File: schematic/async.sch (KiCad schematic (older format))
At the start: 84 parts, among them J1 LOAD, J2 Solar panel, J3 Battery, J4 Screw_Terminal_01x03, J5 Temperature, J7 Screw_Terminal_01x03, J8 USB_B, Q1 IRF4905, Q2 IRF4905, Q3 IRF4905, Q4 2N3904, Q5 2N3904, Q6 IRF4905, Q7 2N3904, Q8 IRF4905, Q9 2N3904, SW1 Backlight control, SW2 RESET, T1 Mains Transformer, U1 ACS712module, U10 ATMEGA328-PU, U11 SD_Micro_5V, U2 IR2110, U3 IR2110, U4 DS18B20, U5 ACS712module, U6 DS18B20, U7 DS1307_RTC, U8 MP2307_DC-DC_module, U9 LCDSerial2004

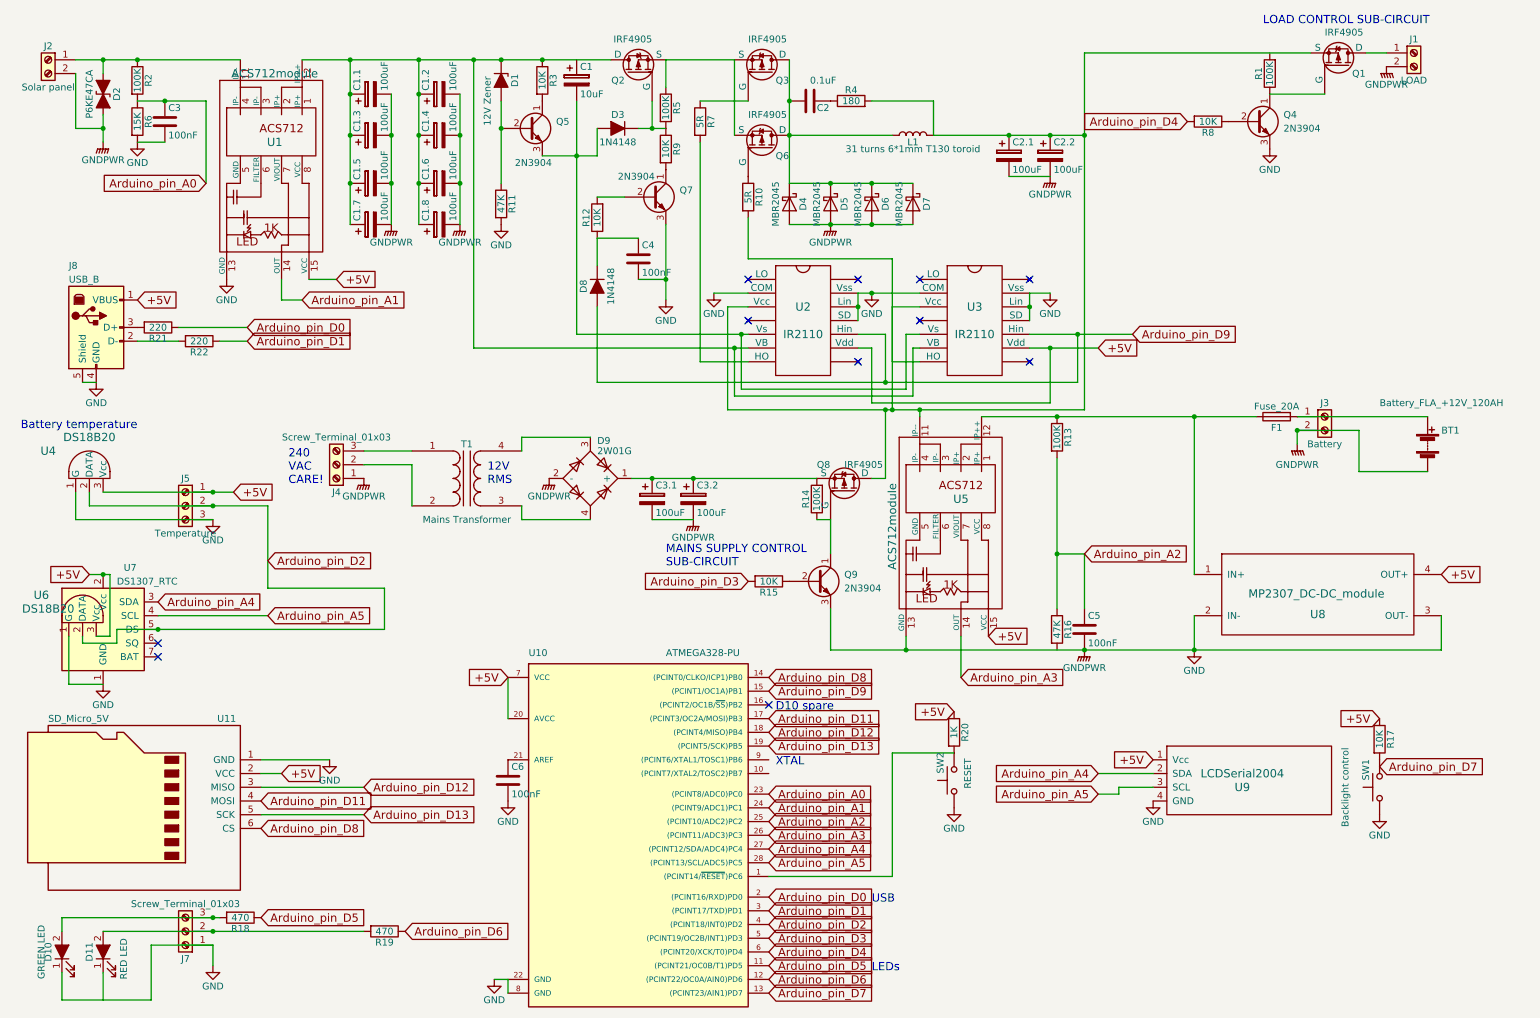
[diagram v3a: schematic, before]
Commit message: added 16 MHz crystal and mains 12V terminals
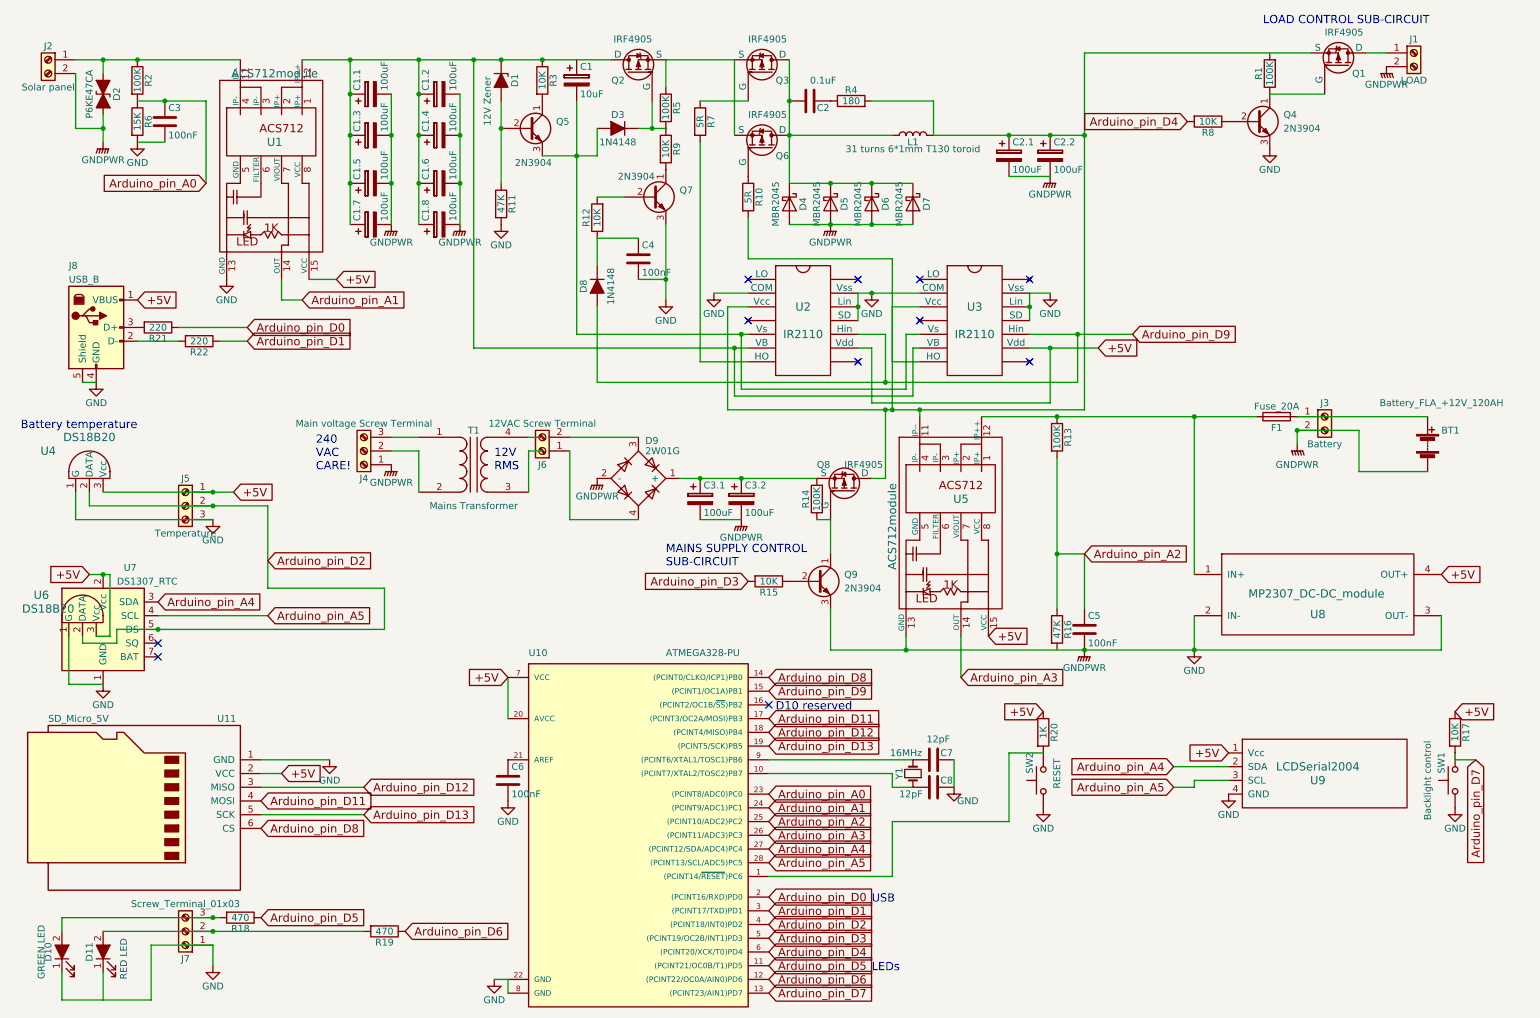
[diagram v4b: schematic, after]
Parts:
- added C7, C8: 12pF, symbol C
- added J6: 12VAC Screw Terminal, symbol Screw_Terminal_01x02
- added Y1: 16MHz, symbol Crystal_Small
- J4: value Screw_Terminal_01x03 -> Main voltage Screw Terminal
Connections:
- net Arduino_pin_D7: now also R17.2, SW1.2
- net GND: now also C7.1, C8.1
- net at U10.10 ((PCINT7/XTAL2/TOSC2)PB7): now also C8.2, Y1.1
- net at U10.9 ((PCINT6/XTAL1/TOSC1)PB6): now also C7.2, Y1.2
- net at T1.3 (SA): no longer D9.4
- net at T1.4 (SB): no longer D9.3
- new net: D9.3, J6.2 (Pin_2)
- new net: D9.4, J6.1 (Pin_1)
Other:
- note added: "D10 reserved"
- note removed: "D10 spare"
- note removed: "XTAL"
- moved on the sheet: C3.1, C3.2, D9, J4, R17, R20, SW1, SW2, T1, U9

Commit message: swapped C1.x and Q1
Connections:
- net at C1.1.1, C1.2.1, C1.3.1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: now also Q2.3 (S), Q3.3 (S), Q6.3 (S), R5.1; no longer D1.1 (K), Q2.1 (D), R3.1, U1.12 (IP++), U2.6 (VB), U3.6 (VB)
- net at C2.1.1, C2.2.1, L1.2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: no longer R10.2, U3.7 (HO)
- new net: D1.1 (K), Q2.1 (D), R3.1, U1.12 (IP++), U2.6 (VB), U3.6 (VB)
- new net: R10.2, U3.7 (HO)
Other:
- moved on the sheet: C1, C1.1, C1.2, C1.3, C1.4, C1.5, C1.6, C1.7, C1.8, C4, D1, D3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

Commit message: updated BOM
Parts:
- renumbered C7 to C10, C8 to C11, C1 to C7, C2 to C8, C3 to C9
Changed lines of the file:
@@
 $EndComp
 $Comp
-L C C3
+L C C9
 U 1 1 5AF665D7
 P 1550 1300
-F 0 "C3" H 1575 1400 50  0000 L CNN
+F 0 "C9" H 1575 1400 50  0000 L CNN
 F 1 "100nF" H 1575 1200 50  0000 L CNN
 F 2 "" H 1588 1150 50  0001 C CNN
@@
 $EndComp
 Wire Wire Line
-	1350 1150 1550 1150
-Wire Wire Line
-	1550 1150 1850 1150
-Wire Wire Line
-	900  850  1100 850
-Wire Wire Line
-	1100 850  1350 850
-Wire Wire Line
-	1350 850  2100 850
+	1350 1150 1850 1150
+Wire Wire Line
+	900  850  2100 850
 $Comp
 L GND #PWR3
@@
 Connection ~ 9800 3550
 Wire Wire Line
-	4300 850  4450 850
-Wire Wire Line
-	4450 850  4950 850
-Wire Wire Line
-	4950 850  5700 850
-Wire Wire Line
-	2550 850  2900 850
-Wire Wire Line
-	2900 850  3100 850
-Wire Wire Line
-	3100 850  3400 850
-Wire Wire Line
-	3400 850  3900 850
+	4300 850  5700 850
+Wire Wire Line
+	2550 850  3900 850
 $Comp
 L GNDPWR #PWR21
@@
 Arduino_pin_D2
 Wire Wire Line
-	1000 4100 1900 4100
-Wire Wire Line
-	1900 4100 2300 4100
+	1000 4100 2300 4100
 $Comp
 L GND #PWR19
@@
 +5V
 Wire Wire Line
-	1100 4000 1900 4000
-Wire Wire Line
-	1900 4000 2050 4000
+	1100 4000 2050 4000
 Wire Wire Line
 	1000 4000 1000 4100
@@
 	900  1350 900  950
 Wire Wire Line
-	1100 1250 1100 1350
-Wire Wire Line
-	1100 1350 1100 1450
+	1100 1250 1100 1450
 Wire Wire Line
 	1100 950  1100 850
@@
 $EndComp
 Wire Wire Line
-	6400 5150 6950 5150
-Wire Wire Line
-	6950 5150 8250 5150
-Wire Wire Line
-	8250 5150 9050 5150
-Wire Wire Line
-	9050 5150 10850 5150
+	6400 5150 10850 5150
 $Comp
 L GND #PWR22
@@
 MAINS SUPPLY CONTROL \nSUB-CIRCUIT
 Wire Wire Line
-	7500 3450 8050 3450
-Wire Wire Line
-	8050 3450 9050 3450
-Wire Wire Line
-	9050 3450 9500 3450
+	7500 3450 9500 3450
 $Comp
 L ACS712module U5
@@
 $EndComp
 Wire Wire Line
-	8050 3750 8050 4450
-Wire Wire Line
-	8050 4450 8050 4850
+	8050 3750 8050 4850
 Wire Wire Line
 	6950 5050 6950 5150
@@
 Arduino_pin_D7
 Wire Wire Line
-	4450 850  4450 1100
-Wire Wire Line
-	4450 1100 4450 1400
-Wire Wire Line
-	4450 1400 4450 1750
-Wire Wire Line
-	4450 1750 4450 2050
+	4450 850  4450 2050
 Connection ~ 4450 1750
 Connection ~ 4450 1400
@@
 Connection ~ 4450 1100
 Wire Wire Line
-	4750 1100 4750 1400
-Wire Wire Line
-	4750 1400 4750 1750
-Wire Wire Line
-	4750 1750 4750 2050
+	4750 1100 4750 2050
 Connection ~ 4750 1400
 Connection ~ 4750 1750
 Wire Wire Line
-	8250 3400 7050 3400
-Wire Wire Line
-	7050 3400 6850 3400
-Wire Wire Line
-	6850 3400 6800 3400
-Wire Wire Line
-	6800 3400 5650 3400
+	8250 3400 5650 3400
 Wire Wire Line
 	7050 3400 7050 3450
@@
 	2300 4700 3150 4700
 Wire Wire Line
-	3150 4700 3150 5000
-Wire Wire Line
-	3150 5000 1500 5000
-Wire Wire Line
-	1500 5000 1200 5000
+	3150 5000 3150 4700
+Wire Wire Line
+	1200 5000 3150 5000
 $Comp
 L DS18B20 U6
@@
 	1050 5050 1150 5050
 Wire Wire Line
-	1150 5050 1150 4600
-Wire Wire Line
-	1150 4600 1100 4600
-Wire Wire Line
-	1100 4600 1000 4600
+	1150 4600 1150 5050
+Wire Wire Line
+	1000 4600 1150 4600
 Wire Wire Line
 	950  5050 950  5100
@@
 $EndComp
 Wire Wire Line
-	800  7100 1900 7100
-Wire Wire Line
-	1900 7100 1950 7100
-Wire Wire Line
-	1100 7200 1900 7200
-Wire Wire Line
-	1900 7200 3000 7200
+	800  7100 1950 7100
+Wire Wire Line
+	1100 7200 3000 7200
 Connection ~ 1900 7200
 Wire Wire Line
@@
 $EndComp
 Wire Wire Line
-	8250 800  8250 1400
-Wire Wire Line
-	8250 1400 8250 3400
+	8250 800  8250 3400
 $Comp
 L ATMEGA328-PU U10
@@
 $EndComp
 $Comp
-L GNDPWR #PWR6
+L GNDPWR #PWR7
 U 1 1 5AFA9065
 P 4750 2050
-F 0 "#PWR6" H 4750 1850 50  0001 C CNN
+F 0 "#PWR7" H 4750 1850 50  0001 C CNN
 F 1 "GNDPWR" H 4750 1920 50  0000 C CNN
 F 2 "" H 4750 2000 50  0001 C CNN
@@
 $EndComp
 Wire Wire Line
-	4100 1350 4200 1350
-Wire Wire Line
-	4200 1350 4300 1350
+	4100 1350 4300 1350
 Wire Wire Line
 	4200 1350 4200 1150
@@
 $EndComp
 Wire Wire Line
-	3100 1150 3100 1350
-Wire Wire Line
-	3100 1350 3100 1750
-$Comp
-L CP C1
+	3100 1150 3100 1750
+$Comp
+L CP C7
 U 1 1 5AFAF73D
 P 3650 1000
-F 0 "C1" H 3675 1100 50  0000 L CNN
+F 0 "C7" H 3675 1100 50  0000 L CNN
 F 1 "10uF" H 3675 900 50  0000 L CNN
 F 2 "" H 3688 850 50  0001 C CNN
@@
 $EndComp
 $Comp
-L GND #PWR8
+L GND #PWR6
 U 1 1 5AFAF73F
 P 3100 2050
-F 0 "#PWR8" H 3100 1800 50  0001 C CNN
+F 0 "#PWR6" H 3100 1800 50  0001 C CNN
 F 1 "GND" H 3100 1900 50  0000 C CNN
 F 2 "" H 3100 2050 50  0001 C CNN
@@
 $EndComp
 Wire Wire Line
-	3400 1550 3650 1550
-Wire Wire Line
-	3650 1550 3800 1550
+	3400 1550 3800 1550
 Wire Wire Line
 	4300 850  4300 1050
@@
 $EndComp
 Wire Wire Line
-	5700 1400 5700 850
-Wire Wire Line
-	6100 850  6100 1150
-Wire Wire Line
-	6100 1150 6100 1400
-Wire Wire Line
-	6100 1400 6100 1750
+	5700 850  5700 1400
+Wire Wire Line
+	6100 850  6100 1750
 Wire Wire Line
 	6100 1400 6850 1400
@@
 $EndComp
 Wire Wire Line
-	6100 1750 6400 1750
-Wire Wire Line
-	6400 1750 6700 1750
-Wire Wire Line
-	6700 1750 7000 1750
+	6100 1750 7000 1750
 Connection ~ 6700 1750
 Connection ~ 6400 1750
 Connection ~ 6100 1400
 Wire Wire Line
-	6100 2050 6400 2050
-Wire Wire Line
-	6400 2050 6700 2050
-Wire Wire Line
-	6700 2050 7000 2050
+	6100 2050 7000 2050
 Connection ~ 6700 2050
 $Comp
-L C C2
+L C C8
 U 1 1 5AFCEF88
 P 6250 1150
-F 0 "C2" V 6300 1200 50  0000 L CNN
+F 0 "C8" V 6300 1200 50  0000 L CNN
 F 1 "0.1uF" V 6100 1150 50  0000 L CNN
 F 2 "" H 6288 1000 50  0001 C CNN
@@
 Connection ~ 7700 1400
 Wire Wire Line
-	7150 1400 7700 1400
-Wire Wire Line
-	7700 1400 8000 1400
-Wire Wire Line
-	8000 1400 8250 1400
+	7150 1400 8250 1400
 Connection ~ 6100 1150
 Connection ~ 5450 3900
@@
 $EndComp
 Wire Wire Line
-	4950 850  4950 1100
-Wire Wire Line
-	4950 1100 4950 1400
-Wire Wire Line
-	4950 1400 4950 1750
-Wire Wire Line
-	4950 1750 4950 2050
+	4950 850  4950 2050
 Connection ~ 4950 1750
 Connection ~ 4950 1400
@@
 Connection ~ 4950 1100
 Wire Wire Line
-	5250 1100 5250 1400
-Wire Wire Line
-	5250 1400 5250 1750
-Wire Wire Line
-	5250 1750 5250 2050
+	5250 1100 5250 2050
 Connection ~ 5250 1400
 Connection ~ 5250 1750
 $Comp
-L GNDPWR #PWR7
+L GNDPWR #PWR8
 U 1 1 5AFDEEAB
 P 5250 2050
-F 0 "#PWR7" H 5250 1850 50  0001 C CNN
+F 0 "#PWR8" H 5250 1850 50  0001 C CNN
 F 1 "GNDPWR" H 5250 1920 50  0000 C CNN
 F 2 "" H 5250 2000 50  0001 C CNN
@@
 Connection ~ 3400 850
 Wire Wire Line
-	3650 2850 5750 2850
-Wire Wire Line
-	5750 2850 5800 2850
-Wire Wire Line
-	3650 1150 3650 1550
-Wire Wire Line
-	3650 1550 3650 2850
+	3650 2850 5800 2850
+Wire Wire Line
+	3650 1150 3650 2850
 Connection ~ 3650 1550
 Wire Wire Line
-	3350 2950 5700 2950
-Wire Wire Line
-	5700 2950 5800 2950
+	3350 2950 5800 2950
 Wire Wire Line
 	2900 2300 2900 850
@@
 Connection ~ 5750 2850
 Wire Wire Line
-	7850 2850 8200 2850
-Wire Wire Line
-	8200 2850 8600 2850
+	7850 2850 8600 2850
 Wire Wire Line
 	6600 2850 6800 2850
@@
 	6800 2850 6800 3200
 Wire Wire Line
-	3800 3200 6800 3200
-Wire Wire Line
-	6800 3200 8200 3200
+	3800 3200 8200 3200
 Wire Wire Line
 	8200 3200 8200 2850
@@
 $EndComp
 Wire Wire Line
-	4300 2050 4300 2450
-Wire Wire Line
-	4300 2450 4300 2600
+	4300 2050 4300 2600
 Wire Wire Line
 	4000 1850 3800 1850
@@
 	6400 4200 6300 4200
 Wire Wire Line
-	7850 2550 7850 2650
-Wire Wire Line
-	7850 2650 7850 2750
+	7850 2550 7850 2750
 $Comp
 L GND #PWR13
@@
 	7850 2550 8000 2550
 Wire Wire Line
-	6600 2550 6600 2650
-Wire Wire Line
-	6600 2650 6600 2750
+	6600 2550 6600 2750
 Connection ~ 6600 2650
 Connection ~ 7850 2650
@@
 $EndComp
 Wire Wire Line
-	6600 2550 6700 2550
-Wire Wire Line
-	6700 2550 7050 2550
+	6600 2550 7050 2550
 Connection ~ 6700 2550
 $Comp
@@
 	8000 3350 8000 2950
 Wire Wire Line
-	7850 2950 8000 2950
-Wire Wire Line
-	8000 2950 8350 2950
+	7850 2950 8350 2950
 Text GLabel 8350 2950 2    60   Input ~ 0
 +5V
@@
 	6850 6150 7000 6150
 $Comp
-L C C7
+L C C10
 U 1 1 5AFBE9DE
 P 7150 5950
-F 0 "C7" V 7100 6000 50  0000 L CNN
+F 0 "C10" V 7100 6000 50  0000 L CNN
 F 1 "12pF" V 7000 5900 50  0000 L CNN
 F 2 "" H 7188 5800 50  0001 C CNN
@@
 $EndComp
 $Comp
-L C C8
+L C C11
 U 1 1 5AFBEAFD
 P 7150 6150
-F 0 "C8" V 7100 6200 50  0000 L CNN
+F 0 "C11" V 7100 6200 50  0000 L CNN
 F 1 "12pF" V 7200 5900 50  0000 L CNN
 F 2 "" H 7188 6000 50  0001 C CNN
@@
 	4200 3700 4300 3700
 Wire Wire Line
-	5300 3900 5450 3900
-Wire Wire Line
-	5450 3900 5750 3900
-Wire Wire Line
-	5750 3900 6300 3900
+	5300 3900 6300 3900
 Wire Wire Line
 	2900 2300 3350 2300

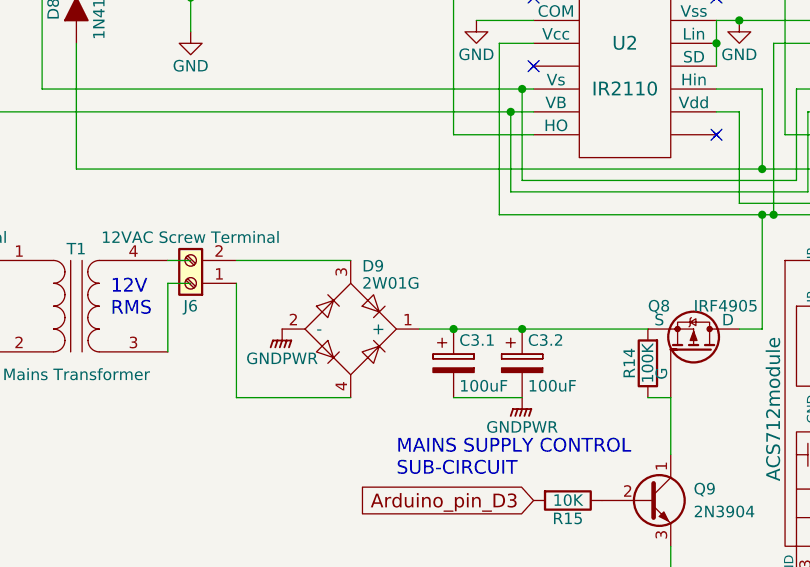
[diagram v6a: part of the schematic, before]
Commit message: bridge rectifier changed to GBJ1506
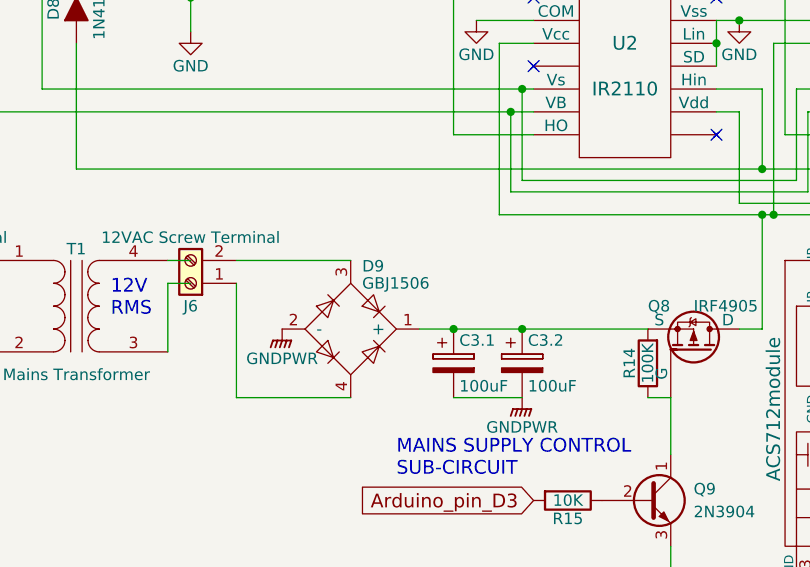
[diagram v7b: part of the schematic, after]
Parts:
- D9: value 2W01G -> GBJ1506
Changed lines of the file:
@@
 P 5000 3900
 F 0 "D9" H 5050 4175 50  0000 L CNN
-F 1 "2W01G" H 5050 4100 50  0000 L CNN
+F 1 "GBJ1506" H 5050 4100 50  0000 L CNN
 F 2 "" H 5000 3900 50  0001 C CNN
 F 3 "" H 5000 3900 50  0001 C CNN
